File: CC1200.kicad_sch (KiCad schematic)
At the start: 54 parts, among them U3 CC1200, U4 MCP6001-OT, U5 MCP41010, X1 40MHz

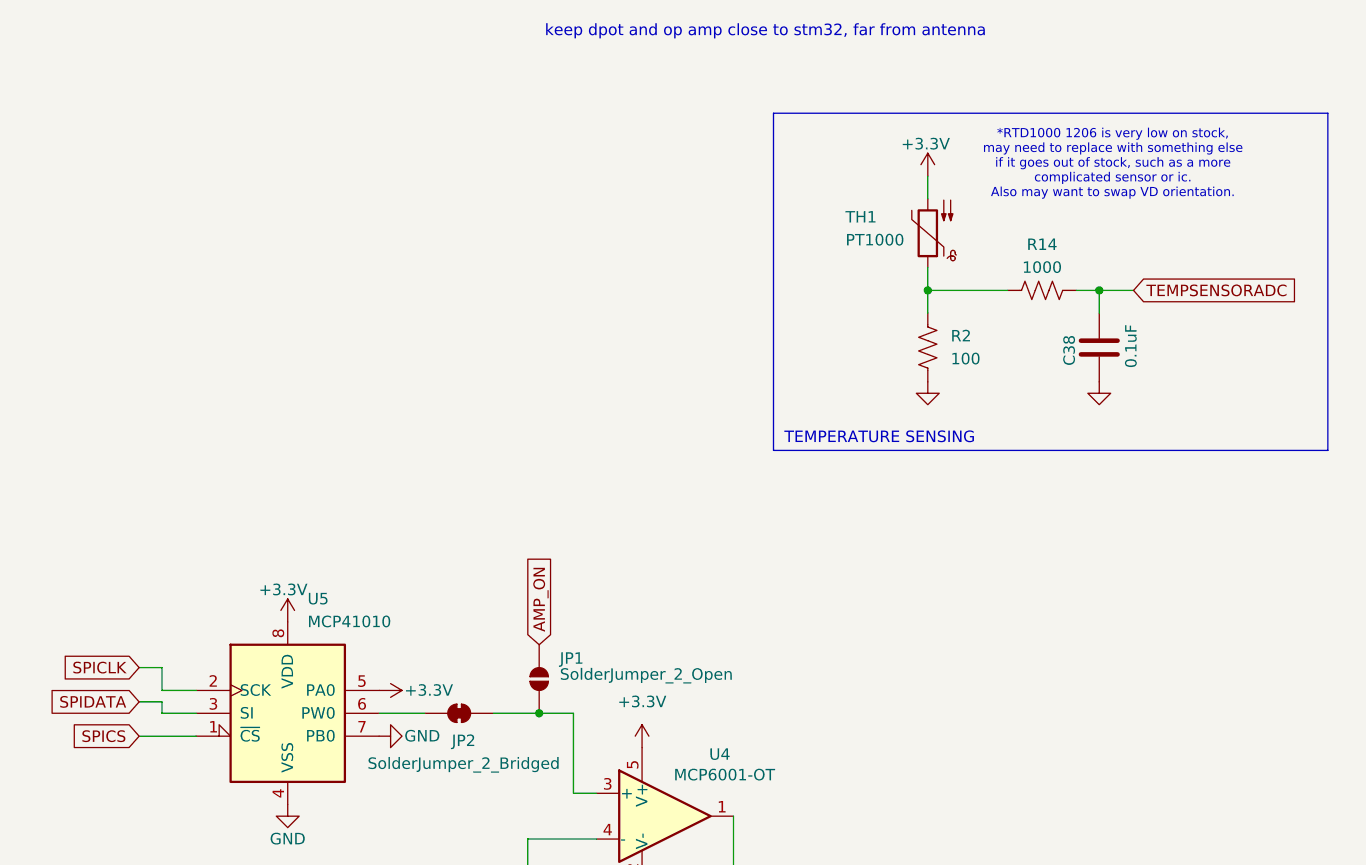
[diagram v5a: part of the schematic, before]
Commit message: added decoupling capacitor to dpot and changed RTD1000 to RTD100
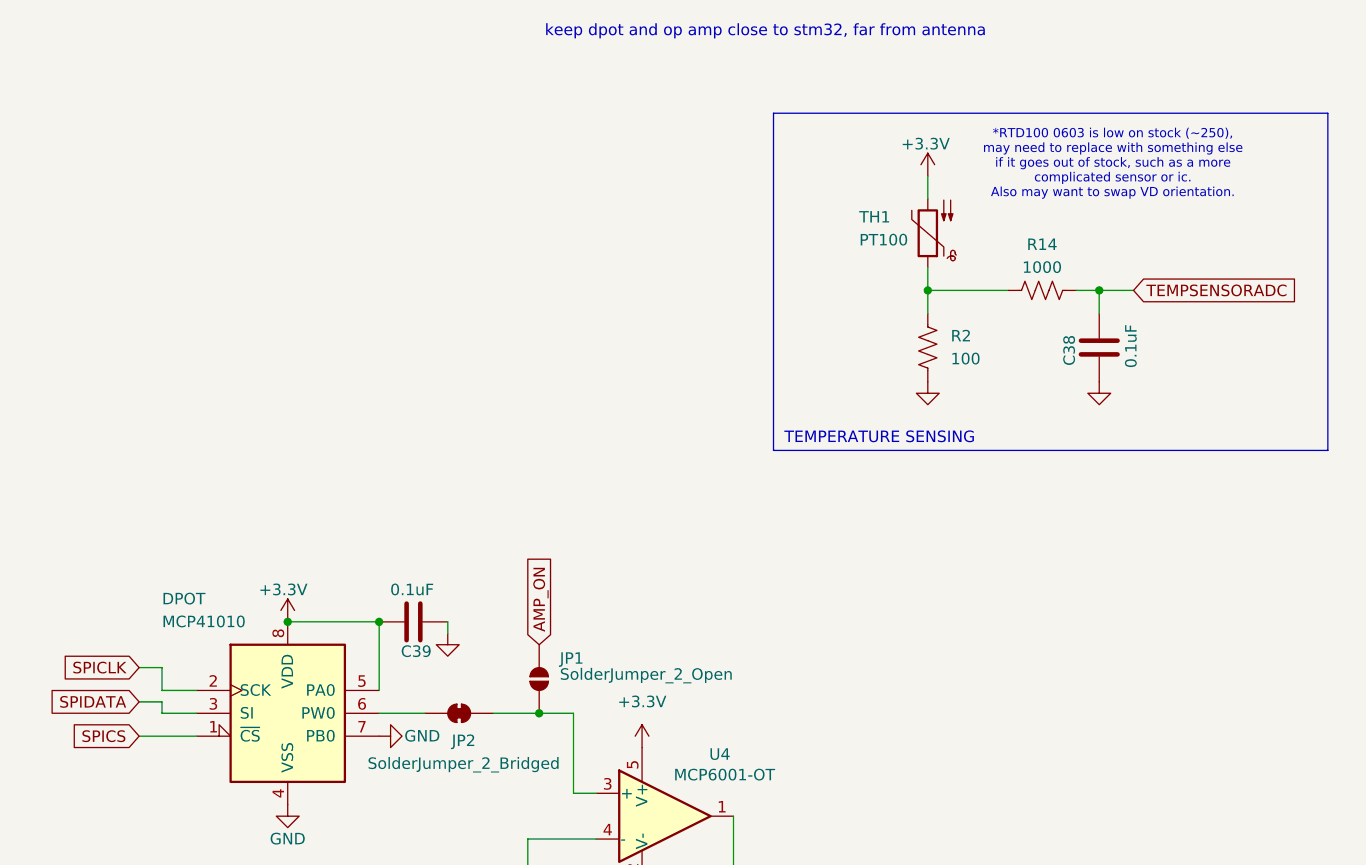
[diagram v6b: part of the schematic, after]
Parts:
- removed TH1: PT1000, Resistor_SMD:R_1206_3216Metric, symbol Sensor_Temperature:PT1000
- added C39: 0.1uF, Capacitor_SMD:C_0402_1005Metric, symbol Device:C
- added TH1: PT100, Resistor_SMD:R_0603_1608Metric, symbol Sensor_Temperature:PT100
- renumbered U5 to DPOT
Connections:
- net +3.3V: now also C39.1, TH1.2
- net GND: now also C39.2
- net at R14.1, R2.1: now also TH1.1
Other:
- note added: "*RTD100 0603 is low on stock (~250), may need to replace with something else if it goes out of stock, such as a more complicated sensor or ic. Also may want to swap VD orientation."
- note removed: "*RTD1000 1206 is very low on stock, may need to replace with something else if it goes out of stock, such as a more complicated sensor or ic. Also may want to swap VD orientation."
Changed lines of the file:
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@@
 	)
 	(junction
+		(at 300.99 86.36)
+		(diameter 0)
+		(color 0 0 0 0)
+	)
+	(junction
 		(at 179.07 82.55)
 		(diameter 0)
@@
 	)
 	(junction
+		(at 290.83 86.36)
+		(diameter 0)
+		(color 0 0 0 0)
+	)
+	(junction
 		(at 147.32 100.33)
 		(diameter 0)
@@
 	(wire
 		(pts
+			(xy 300.99 93.98) (xy 300.99 86.36)
+		)
+		(stroke
+			(width 0)
+			(type default)
+		)
+	)
+	(wire
+		(pts
 			(xy 276.86 93.98) (xy 276.86 91.44)
 		)
@@
 	(wire
 		(pts
+			(xy 308.61 86.36) (xy 308.61 87.63)
+		)
+		(stroke
+			(width 0)
+			(type default)
+		)
+	)
+	(wire
+		(pts
 			(xy 34.29 90.17) (xy 64.77 90.17)
 		)
@@
 	(wire
 		(pts
+			(xy 300.99 86.36) (xy 290.83 86.36)
+		)
+		(stroke
+			(width 0)
+			(type default)
+		)
+	)
+	(wire
+		(pts
 			(xy 64.77 120.65) (xy 59.69 120.65)
 		)
@@
 		)
 	)
-	(text "*RTD1000 1206 is very low on stock, \nmay need to replace with something else\nif it goes out of stock, such as a more \ncomplicated sensor or ic.\nAlso may want to swap VD orientation."
+	(text "*RTD100 0603 is low on stock (~250), \nmay need to replace with something else\nif it goes out of stock, such as a more \ncomplicated sensor or ic.\nAlso may want to swap VD orientation."
 		(exclude_from_sim no)
 		(at 382.524 35.56 0)
@@
 		(on_board yes)
 		(dnp no)
-		(fields_autoplaced yes)
-		(property "Reference" "U5"
-			(at 293.0241 83.82 0)
+		(property "Reference" "DPOT"
+			(at 276.86 83.82 0)
 			(effects
 				(font
@@
 		)
 		(property "Value" "MCP41010"
-			(at 293.0241 86.36 0)
+			(at 276.86 86.36 0)
 			(effects
 				(font
@@
 			(project ""
 				(path "/4108571e-8c4c-4eba-a51f-04b21c4cec35/dfcafdf4-f213-4518-865d-ab9ee2b88e54"
-					(reference "U5")
+					(reference "DPOT")
 					(unit 1)
 				)
@@
 	(symbol
 		(lib_id "Device:C")
+		(at 304.8 86.36 90)
+		(unit 1)
+		(exclude_from_sim no)
+		(in_bom yes)
+		(on_board yes)
+		(dnp no)
+		(property "Reference" "C39"
+			(at 306.832 89.662 90)
+			(effects
+				(font
+					(size 1.27 1.27)
+				)
+				(justify left)
+			)
+		)
+		(property "Value" "0.1uF"
+			(at 307.086 82.804 90)
+			(effects
+				(font
+					(size 1.27 1.27)
+				)
+				(justify left)
+			)
+		)
+		(property "Footprint" "Capacitor_SMD:C_0402_1005Metric"
+			(at 308.61 85.3948 0)
+			(effects
+				(font
+					(size 1.27 1.27)
+				)
+				(hide yes)
+			)
+		)
+		(property "Datasheet" "https://jlcpcb.com/api/file/downloadByFileSystemAccessId/8579707269996871680"
+			(at 304.8 86.36 0)
+			(effects
+				(font
+					(size 1.27 1.27)
+				)
+				(hide yes)
+			)
+		)
+		(property "Description" ""
+			(at 304.8 86.36 0)
+			(effects
+				(font
+					(size 1.27 1.27)
+				)
+				(hide yes)
+			)
+		)
+		(property "LCSC" "C1525"
+			(at 304.8 86.36 0)
+			(effects
+				(font
+					(size 1.27 1.27)
+				)
+				(hide yes)
+			)
+		)
+		(pin "1"
+		)
+		(pin "2"
+		)
+		(instances
+			(project "rocketBeaconModule"
+				(path "/4108571e-8c4c-4eba-a51f-04b21c4cec35/dfcafdf4-f213-4518-865d-ab9ee2b88e54"
+					(reference "C39")
+					(unit 1)
+				)
+			)
+		)
+	)
+	(symbol
+		(lib_id "Sensor_Temperature:PT100")
+		(at 361.95 43.18 180)
+		(unit 1)
+		(exclude_from_sim no)
+		(in_bom yes)
+		(on_board yes)
+		(dnp no)
+		(property "Reference" "TH1"
+			(at 354.33 41.402 0)
+			(effects
+				(font
+					(size 1.27 1.27)
+				)
+				(justify right)
+			)
+		)
+		(property "Value" "PT100"
+			(at 354.33 43.942 0)
+			(effects
+				(font
+					(size 1.27 1.27)
+				)
+				(justify right)
+			)
+		)
+		(property "Footprint" "Resistor_SMD:R_0603_1608Metric"
+			(at 361.95 44.45 0)
+			(effects
+				(font
+					(size 1.27 1.27)
+				)
+				(hide yes)
+			)
+		)
+		(property "Datasheet" "https://jlcpcb.com/api/file/downloadByFileSystemAccessId/8588899961215307776"
+			(at 361.95 44.45 0)
+			(effects
+				(font
+					(size 1.27 1.27)
+				)
+				(hide yes)
+			)
+		)
+		(property "Description" "PT100 platinum temperature sensor (RTD)"
+			(at 361.95 43.18 0)
+			(effects
+				(font
+					(size 1.27 1.27)
+				)
+				(hide yes)
+			)
+		)
+		(property "LCSC" "C141518"
+			(at 361.95 43.18 0)
+			(effects
+				(font
+					(size 1.27 1.27)
+				)
+				(hide yes)
+			)
+		)
+		(pin "1"
+		)
+		(pin "2"
+		)
+		(instances
+			(project ""
+				(path "/4108571e-8c4c-4eba-a51f-04b21c4cec35/dfcafdf4-f213-4518-865d-ab9ee2b88e54"
+					(reference "TH1")
+					(unit 1)
+				)
+			)
+		)
+	)
+	(symbol
+		(lib_id "Device:C")
 		(at 118.11 93.98 270)
 		(unit 1)
@@
 	)
 	(symbol
+		(lib_name "GND_4")
+		(lib_id "power:GND")
+		(at 308.61 87.63 0)
+		(unit 1)
+		(exclude_from_sim no)
+		(in_bom yes)
+		(on_board yes)
+		(dnp no)
+		(fields_autoplaced yes)
+		(property "Reference" "#PWR017"
+			(at 308.61 93.98 0)
+			(effects
+				(font
+					(size 1.27 1.27)
+				)
+				(hide yes)
+			)
+		)
+		(property "Value" "GND"
+			(at 308.61 92.71 0)
+			(effects
+				(font
+					(size 1.27 1.27)
+				)
+				(hide yes)
+			)
+		)
+		(property "Footprint" ""
+			(at 308.61 87.63 0)
+			(effects
+				(font
+					(size 1.27 1.27)
+				)
+				(hide yes)
+			)
+		)
+		(property "Datasheet" ""
+			(at 308.61 87.63 0)
+			(effects
+				(font
+					(size 1.27 1.27)
+				)
+				(hide yes)
+			)
+		)
+		(property "Description" "Power symbol creates a global label with name \"GND\" , ground"
+			(at 308.61 87.63 0)
+			(effects
+				(font
+					(size 1.27 1.27)
+				)
+				(hide yes)
+			)
+		)
+		(pin "1"
+		)
+		(instances
+			(project ""
+				(path "/4108571e-8c4c-4eba-a51f-04b21c4cec35/dfcafdf4-f213-4518-865d-ab9ee2b88e54"
+					(reference "#PWR017")
+					(unit 1)
+				)
+			)
+		)
+	)
+	(symbol
 		(lib_id "Device:C")
 		(at 106.68 113.03 270)
@@
 					(unit 1)
 				)
-			)
-		)
-	)
-	(symbol
-		(lib_id "Sensor_Temperature:PT1000")
-		(at 361.95 43.18 180)
-		(unit 1)
-		(exclude_from_sim no)
-		(in_bom yes)
-		(on_board yes)
-		(dnp no)
-		(property "Reference" "TH1"
-			(at 352.806 41.402 0)
-			(effects
-				(font
-					(size 1.27 1.27)
-				)
-				(justify right)
-			)
-		)
-		(property "Value" "PT1000"
-			(at 352.806 43.942 0)
-			(effects
-				(font
-					(size 1.27 1.27)
-				)
-				(justify right)
-			)
-		)
-		(property "Footprint" "Resistor_SMD:R_1206_3216Metric"
-			(at 361.95 44.45 0)
-			(effects
-				(font
-					(size 1.27 1.27)
-				)
-				(hide yes)
-			)
-		)
-		(property "Datasheet" "https://jlcpcb.com/api/file/downloadByFileSystemAccessId/8588899961207730176"
-			(at 361.95 44.45 0)
-			(effects
-				(font
-					(size 1.27 1.27)
-				)
-				(hide yes)
-			)
-		)
-		(property "Description" "PT1000 platinum temperature sensor (RTD)"
-			(at 361.95 43.18 0)
-			(effects
-				(font
-					(size 1.27 1.27)
-				)
-				(hide yes)
-			)
-		)
-		(property "LCSC" "C141528"
-			(at 361.95 43.18 0)
-			(effects
-				(font
-					(size 1.27 1.27)
-				)
-				(hide yes)
-			)
-		)
-		(pin "2"
-		)
-		(pin "1"
-		)
-		(instances
-			(project ""
-				(path "/4108571e-8c4c-4eba-a51f-04b21c4cec35/dfcafdf4-f213-4518-865d-ab9ee2b88e54"
-					(reference "TH1")
-					(unit 1)
-				)
-			)
-		)
-	)
-	(symbol
-		(lib_name "+3.3V_4")
-		(lib_id "power:+3.3V")
-		(at 300.99 93.98 270)
-		(unit 1)
-		(exclude_from_sim no)
-		(in_bom yes)
-		(on_board yes)
-		(dnp no)
-		(property "Reference" "#PWR025"
-			(at 297.18 93.98 0)
-			(effects
-				(font
-					(size 1.27 1.27)
-				)
-				(hide yes)
-			)
-		)
-		(property "Value" "+3.3V"
-			(at 303.784 93.98 90)
-			(effects
-				(font
-					(size 1.27 1.27)
-				)
-				(justify left)
-			)
-		)
-		(property "Footprint" ""
-			(at 300.99 93.98 0)
-			(effects
-				(font
-					(size 1.27 1.27)
-				)
-				(hide yes)
-			)
-		)
-		(property "Datasheet" ""
-			(at 300.99 93.98 0)
-			(effects
-				(font
-					(size 1.27 1.27)
-				)
-				(hide yes)
-			)
-		)
-		(property "Description" "Power symbol creates a global label with name \"+3.3V\""
-			(at 300.99 93.98 0)
-			(effects
-				(font
-					(size 1.27 1.27)
-				)
-				(hide yes)
-			)
-		)
-		(pin "1"
-		)
-		(instances
-			(project ""
-				(path "/4108571e-8c4c-4eba-a51f-04b21c4cec35/dfcafdf4-f213-4518-865d-ab9ee2b88e54"
-					(reference "#PWR025")
-					(unit 1)
-				)
